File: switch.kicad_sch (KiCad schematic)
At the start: 3 parts

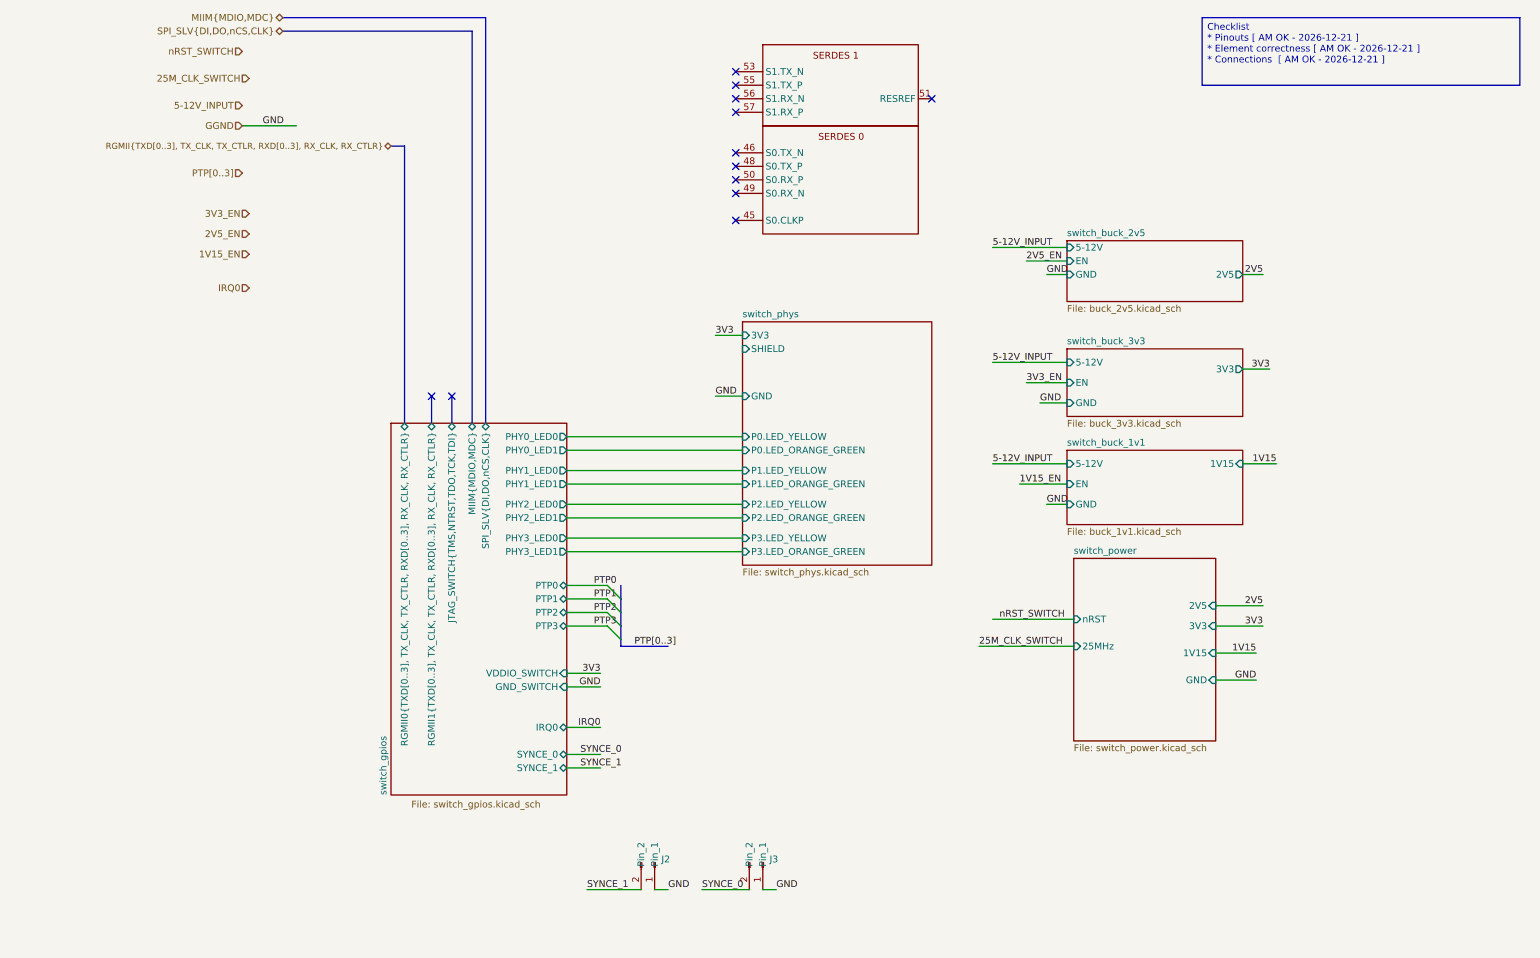
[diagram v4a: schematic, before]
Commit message: This commit intends to fix multiple issues:
 - 1.1 -> 1.15 v buck rails
 - Revision consistently using Rev. A
 - Issue with the Switch symbol when moving library
 - Adding new footprint and symbol for 2.54mm Headers
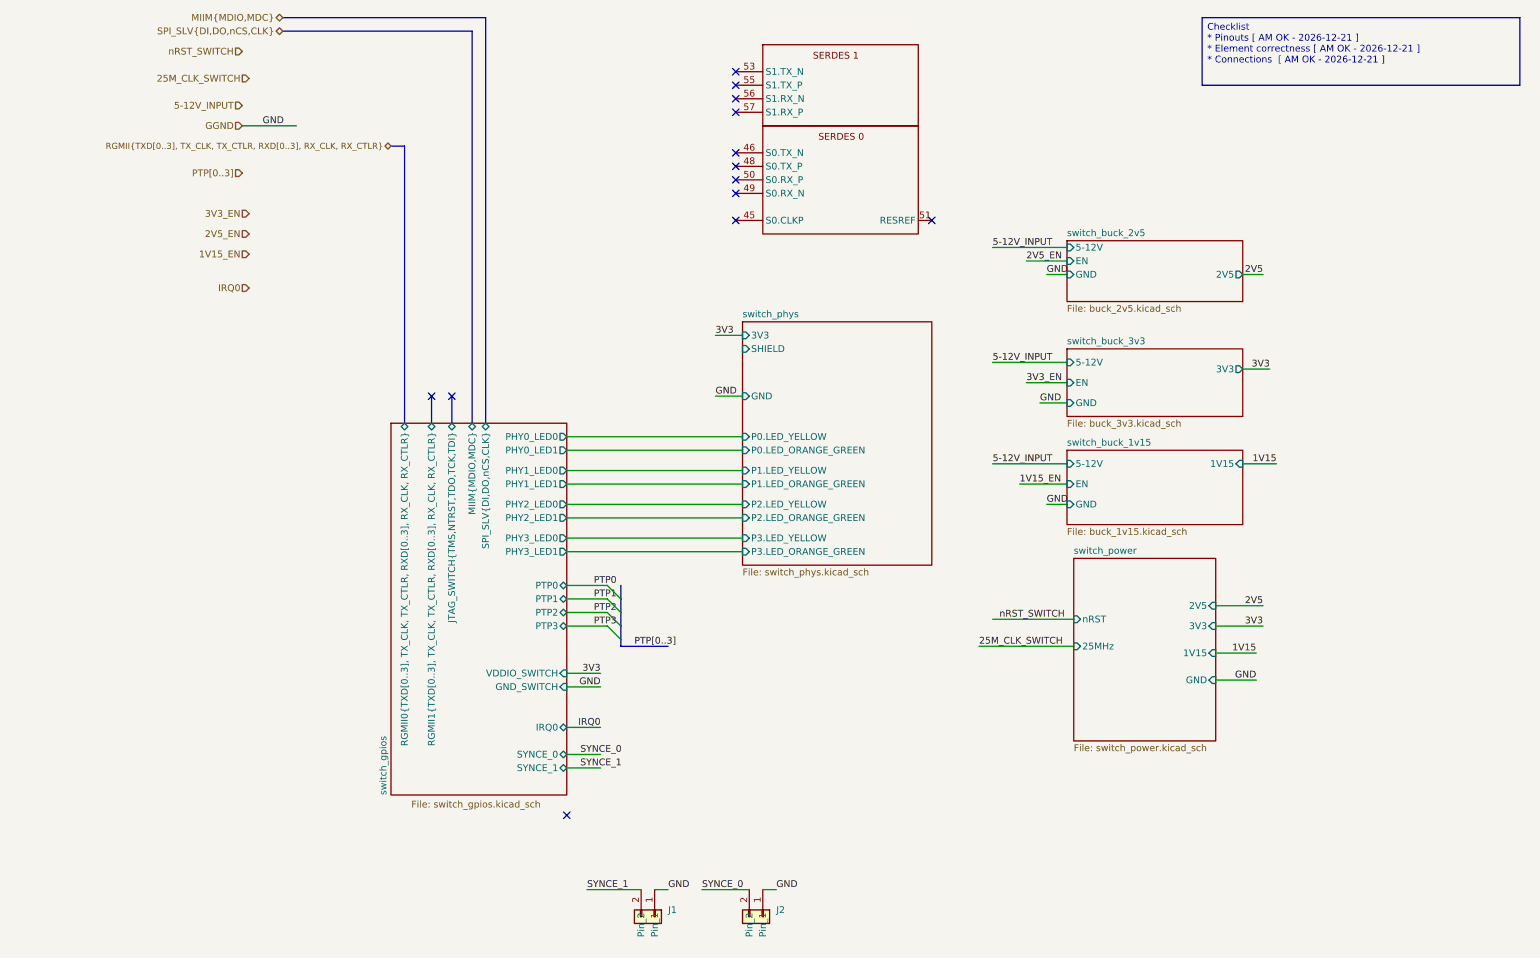
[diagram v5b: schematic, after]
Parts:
- removed J2, J3: ~, KL:PinHeader_1x2_2.54mm, symbol KL_Connector_Headers:1x2_Pin_Header
- added J1, J2: ~, symbol KL_Headers:02x01_2.54mm_Header
- U1: footprint KL:TQFP-128_14x14mm_P0.4mm_with_EPAD -> Package_QFP:TQFP-128_14x14mm_P0.4mm; Digikey 150-LAN96455FT-I/8MWTR-ND -> (none); Mouser 579-LAN96455FTI8MW -> (none); manf# (none) -> LAN96455F-I/8MW
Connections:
- net GGND: now also J1.1 (Pin_1), J2.1 (Pin_1)
- net SYNCE_0: now also J2.2 (Pin_2)
- net SYNCE_1: now also J1.2 (Pin_2)
- no-connect marks 12 -> 13
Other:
- sheet switch_buck_1v1 renamed switch_buck_1v15
- sheet switch_buck_1v15: file buck_1v1.kicad_sch -> buck_1v15.kicad_sch

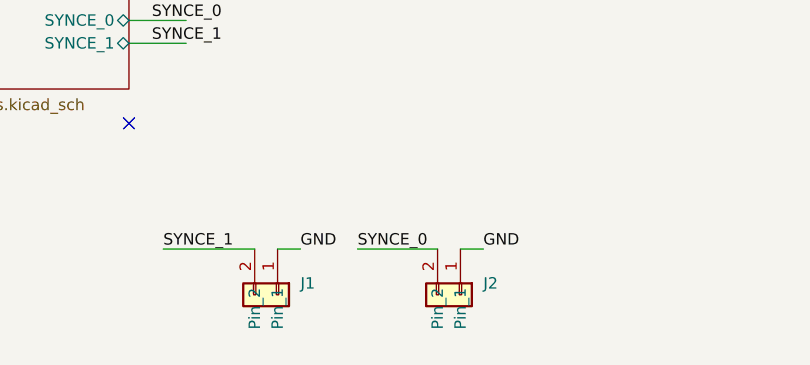
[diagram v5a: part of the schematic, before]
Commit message: switch: annotations on switch IC and connectors
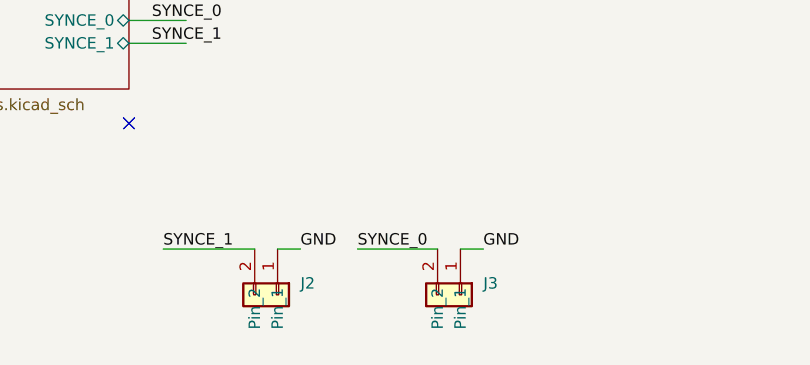
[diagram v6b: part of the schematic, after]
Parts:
- renumbered J1 to J2, J2 to J3
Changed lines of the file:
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@@
 		(dnp no)
 		(fields_autoplaced yes)
-		(property "Reference" "J?"
+		(property "Reference" "J2"
 			(at 120.65 184.1499 90)
 			(effects
@@
 			(project "shish-lan"
 				(path "/d4536448-b109-4159-96e2-3dc21baf2d6e/0b7d9af9-83c1-43fa-a7a0-a33d0a00ea9c"
-					(reference "J?")
+					(reference "J2")
 					(unit 1)
 				)
@@
 		(dnp no)
 		(fields_autoplaced yes)
-		(property "Reference" "J?"
+		(property "Reference" "J3"
 			(at 140.97 184.1499 90)
 			(effects
@@
 			(project "shish-lan"
 				(path "/d4536448-b109-4159-96e2-3dc21baf2d6e/0b7d9af9-83c1-43fa-a7a0-a33d0a00ea9c"
-					(reference "J?")
+					(reference "J3")
 					(unit 1)
 				)
@@
 		(dnp no)
 		(fields_autoplaced yes)
-		(property "Reference" "U?"
+		(property "Reference" "U1"
 			(at 153.67 0 0)
 			(effects
@@
 			(project "shish-lan"
 				(path "/d4536448-b109-4159-96e2-3dc21baf2d6e/0b7d9af9-83c1-43fa-a7a0-a33d0a00ea9c"
-					(reference "U?")
+					(reference "U1")
 					(unit 4)
 				)

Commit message: fixing issue related to symbol changes, and updating components
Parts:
- J2, J3: footprint (none) -> KL:02x01_2.54mm_Header
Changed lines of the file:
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@@
 			)
 		)
-		(property "Footprint" ""
+		(property "Footprint" "KL:02x01_2.54mm_Header"
 			(at 116.84 185.42 0)
 			(effects
@@
 			)
 		)
-		(property "Footprint" ""
+		(property "Footprint" "KL:02x01_2.54mm_Header"
 			(at 137.16 185.42 0)
 			(effects

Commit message: updates all symbols to the project only paths. My bad - sorry
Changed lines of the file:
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@@
 		(fields_autoplaced yes)
 		(property "Reference" "J2"
-			(at 120.65 184.1499 90)
+			(at 120.65 185.4199 90)
 			(effects
 				(font
@@
 		)
 		(property "Value" "~"
-			(at 120.65 186.6899 90)
+			(at 116.84 185.42 0)
 			(effects
 				(font
 					(size 1.27 1.27)
 				)
-				(justify left)
 			)
 		)
@@
 		(fields_autoplaced yes)
 		(property "Reference" "J3"
-			(at 140.97 184.1499 90)
+			(at 140.97 185.4199 90)
 			(effects
 				(font
@@
 		)
 		(property "Value" "~"
-			(at 140.97 186.6899 90)
+			(at 137.16 185.42 0)
 			(effects
 				(font
 					(size 1.27 1.27)
 				)
-				(justify left)
 			)
 		)
@@
 		)
 		(property "Value" "~"
-			(at 168.91 27.9399 0)
+			(at 138.43 21.59 0)
 			(effects
 				(font
 					(size 1.27 1.27)
 				)
-				(justify left)
 			)
 		)
